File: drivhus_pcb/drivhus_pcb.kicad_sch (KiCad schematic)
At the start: 80 parts, among them J1 Setup, J10 RS-485 Right Bus, J11 Temp/Humid/Light Indoors, J12 Temp/Humid Outdoors, J13 Pump 1-4, J14 Pump 5-8, J15 Pump 9-12, J16 Pump 13-15, J2 Conn_01x19_Female, J3 Conn_01x19_Female, J4 RS-485 Left Bus, J5 Conn_Coaxial_Power, J6 +12V, J7 -12V, J8 +5V, J9 -5V, K1 SANYOU_SRD_Form_C, K10 SANYOU_SRD_Form_C, K11 SANYOU_SRD_Form_C, K12 SANYOU_SRD_Form_C, K13 SANYOU_SRD_Form_C, K14 SANYOU_SRD_Form_C, K15 SANYOU_SRD_Form_C, K2 SANYOU_SRD_Form_C, K3 SANYOU_SRD_Form_C, K4 SANYOU_SRD_Form_C, K5 SANYOU_SRD_Form_C, K6 SANYOU_SRD_Form_C, K7 SANYOU_SRD_Form_C, K8 SANYOU_SRD_Form_C, K9 SANYOU_SRD_Form_C, Q1 BC817, Q10 BC817, Q11 BC817, Q12 BC817, Q13 BC817, Q14 BC817, Q15 BC817, Q2 BC817, Q3 BC817, Q4 BC817, Q5 BC817, Q6 BC817, Q7 BC817, Q8 BC817, Q9 BC817, U1 SP3485EN, U2 CD74HC4067M

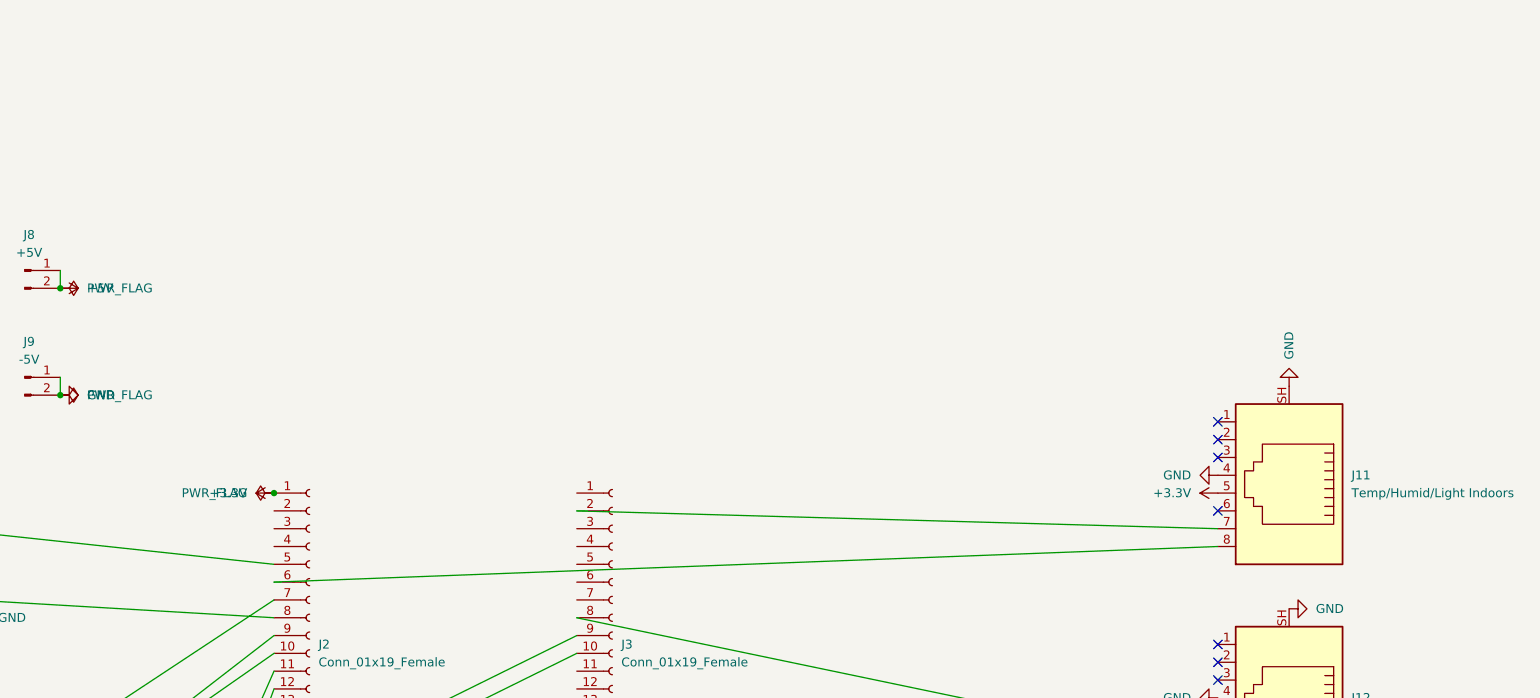
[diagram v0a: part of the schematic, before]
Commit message: Added schematics and PCB for waterlevel switches
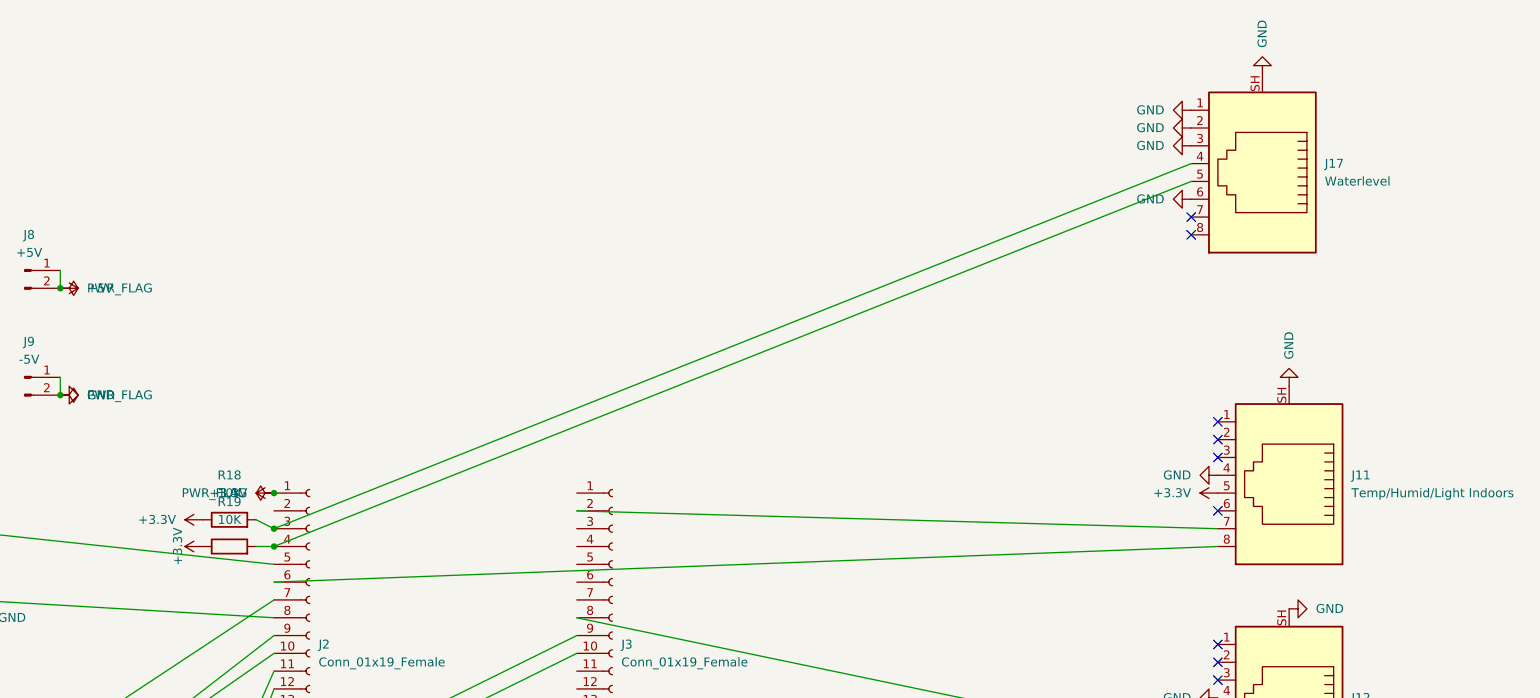
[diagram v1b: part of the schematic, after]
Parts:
- added J17: Waterlevel, Connector_RJ:RJ45_Ninigi_GE, symbol Connector:RJ45_Shielded
- added R18, R19: 10K, Resistor_SMD:R_1206_3216Metric, symbol Device:R
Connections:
- net +3.3V: now also R18.1, R19.1
- net GND: now also J17.1, J17.2, J17.3, J17.6, J17.SH
- net at J2.3 (Pin_3): now also J17.4, R18.2
- net at J2.4 (Pin_4): now also J17.5, R19.2
- no-connect marks 34 -> 36

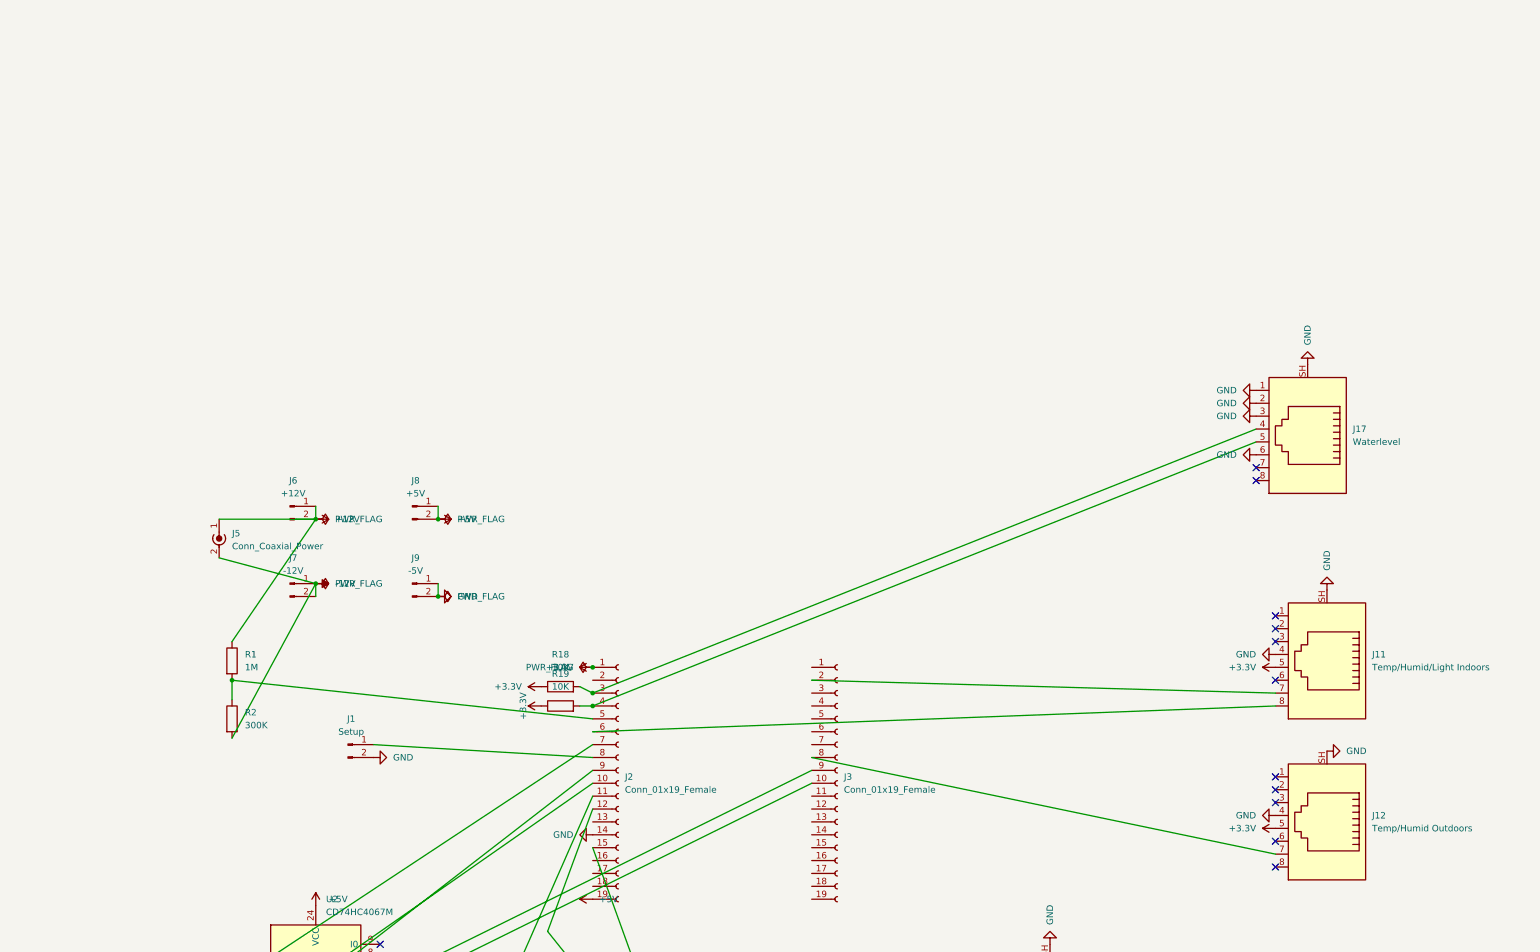
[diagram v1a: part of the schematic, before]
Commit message: Added remaining parts and connections to schematics
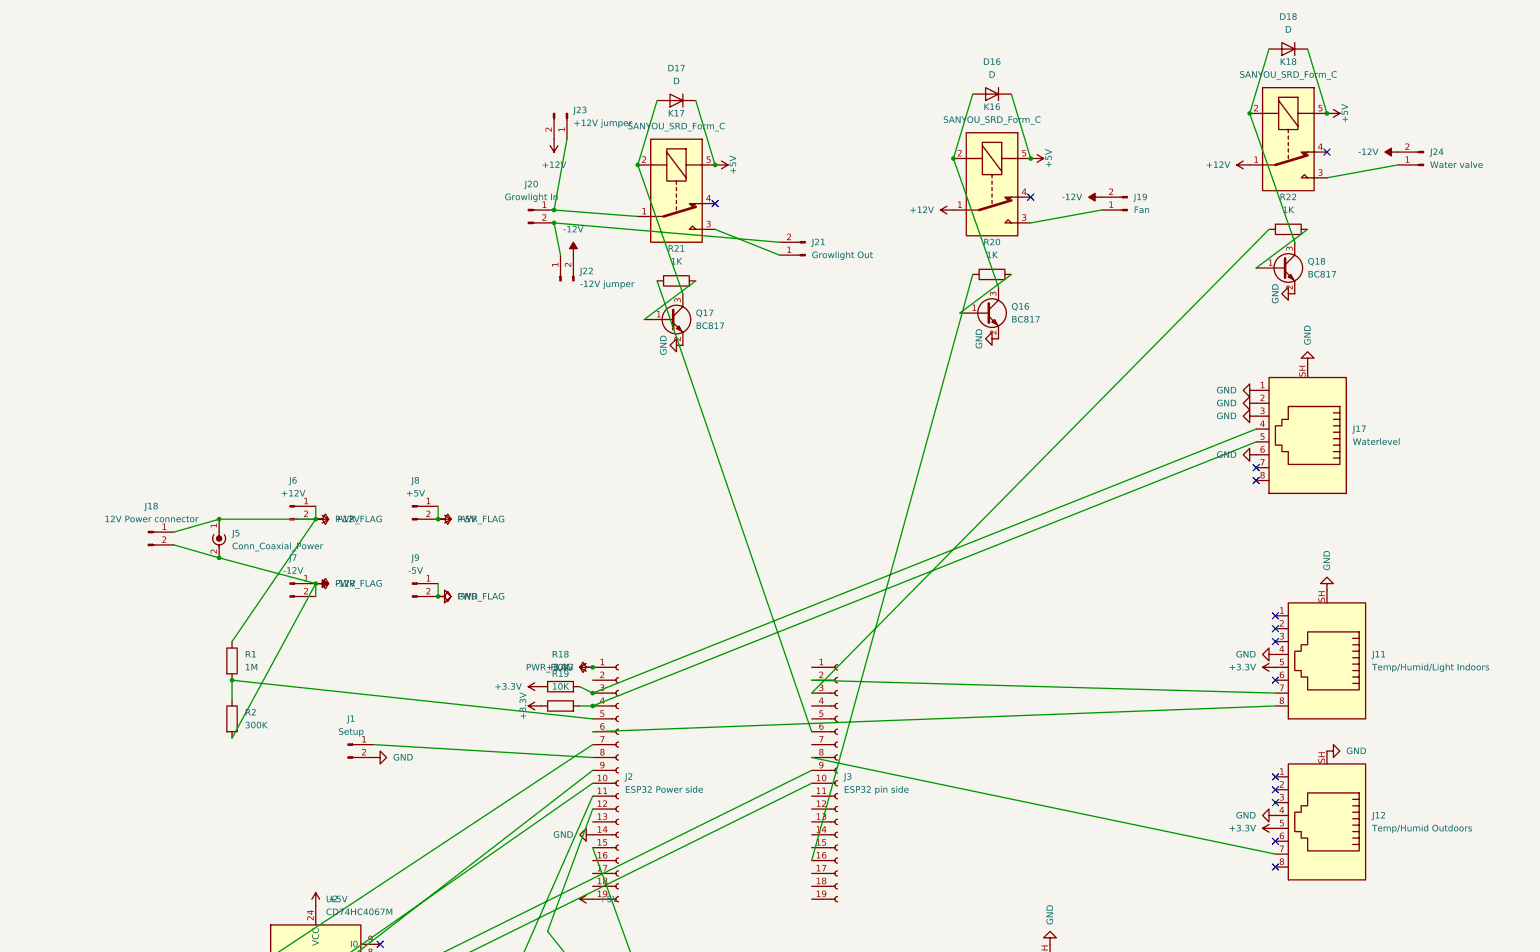
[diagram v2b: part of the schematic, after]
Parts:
- added D16, D17, D18: D, Diode_SMD:D_SMB, symbol Device:D
- added J18: 12V Power connector, TerminalBlock:TerminalBlock_bornier-2_P5.08mm, symbol Connector:Conn_01x02_Male
- added J19: Fan, TerminalBlock:TerminalBlock_bornier-2_P5.08mm, symbol Connector:Conn_01x02_Male
- added J20: Growlight In, TerminalBlock:TerminalBlock_bornier-2_P5.08mm, symbol Connector:Conn_01x02_Male
- added J21: Growlight Out, TerminalBlock:TerminalBlock_bornier-2_P5.08mm, symbol Connector:Conn_01x02_Male
- added J22: -12V jumper, Connector_PinHeader_2.54mm:PinHeader_1x02_P2.54mm_Vertical, symbol Connector:Conn_01x02_Male
- added J23: +12V jumper, Connector_PinHeader_2.54mm:PinHeader_1x02_P2.54mm_Vertical, symbol Connector:Conn_01x02_Male
- added J24: Water valve, TerminalBlock:TerminalBlock_bornier-2_P5.08mm, symbol Connector:Conn_01x02_Male
- added K16, K17, K18: SANYOU_SRD_Form_C, Relay_THT:Relay_SPDT_SANYOU_SRD_Series_Form_C, symbol Relay:SANYOU_SRD_Form_C
- added Q16, Q17, Q18: BC817, Package_TO_SOT_SMD:SOT-23, symbol Transistor_BJT:BC817
- added R20, R21, R22: 1K, Resistor_SMD:R_1206_3216Metric, symbol Device:R
- J1: footprint Resistor_SMD:R_1206_3216Metric -> Connector_PinHeader_2.54mm:PinHeader_1x02_P2.54mm_Vertical
- J2: value Conn_01x19_Female -> ESP32 Power side
- J3: value Conn_01x19_Female -> ESP32 pin side
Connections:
- net +12V: now also J18.1 (Pin_1), J23.2 (Pin_2), K16.1, K18.1
- net +5V: now also D16.1 (K), D17.1 (K), D18.1 (K), K16.5, K17.5, K18.5
- net -12V: now also J18.2 (Pin_2), J19.2 (Pin_2), J22.2 (Pin_2), J24.2 (Pin_2)
- net GND: now also Q16.2 (E), Q17.2 (E), Q18.2 (E)
- net at J3.16 (Pin_16): now also R20.1
- net at J3.3 (Pin_3): now also R22.1
- net at J3.6 (Pin_6): now also R21.1
- new net: D16.2 (A), K16.2, Q16.3 (C)
- new net: J19.1 (Pin_1), K16.3
- new net: J20.1 (Pin_1), J23.1 (Pin_1), K17.1
- new net: J20.2 (Pin_2), J21.2 (Pin_2), J22.1 (Pin_1)
- new net: Q17.1 (B), R21.2
- new net: Q16.1 (B), R20.2
- new net: D17.2 (A), K17.2, Q17.3 (C)
- new net: J21.1 (Pin_1), K17.3
- new net: D18.2 (A), K18.2, Q18.3 (C)
- new net: J24.1 (Pin_1), K18.3
- new net: Q18.1 (B), R22.2
- no-connect marks 36 -> 39
